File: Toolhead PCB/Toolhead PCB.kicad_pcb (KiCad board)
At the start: 2 copper layers, 37.6 x 23.5 mm, 10 parts, among them J1 PicoA, J10 Conn_02x04_Odd_Even, J2 PicoB, J3 PicoC, J4 Heater, J5 Thermistor, J6 Heatbreak Fan, J7 Part Fan, J8 IR/ADXL, J9 MicroProbe

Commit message: Moved the hole for the capacitor down by 0.4mm, and enlarged diameter by 0.5mm. Updated Edge Cuts circle to match. Exported Gerbers and Excellon files. Basic FlatCAM with B_Cu.gbr, Edge_Cuts.gbr, and PTH.drl mirrored along X axis of Edge_Cuts.gbr. Added Alignment Holes. Set Origin.
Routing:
- net Net-(J3-Pin_6): vias 0 -> 1
- net (no net): vias 3 -> 2
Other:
- outline, holes or cut-outs redrawn
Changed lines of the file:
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@@
 	)
 	(gr_circle
-		(center 117.45 52.4)
-		(end 119.5 52.4)
+		(center 117.45 52.8)
+		(end 119.75 52.8)
 		(stroke
 			(width 0.05)
-			(type default)
+			(type solid)
 		)
 		(fill no)
@@
 	(via
 		(at 126.25 65.5)
-		(size 3.126)
+		(size 3.125001)
 		(drill 3.125)
 		(layers "F.Cu" "B.Cu")
@@
 	)
 	(via
-		(at 117.45 52.4)
-		(size 4.001)
-		(drill 4)
-		(layers "F.Cu" "B.Cu")
-		(net 0)
-	)
-	(via
 		(at 107.75 65.5)
-		(size 3.126)
+		(size 3.125001)
 		(drill 3.125)
 		(layers "F.Cu" "B.Cu")
@@
 		(net 5)
 	)
+	(via
+		(at 117.45 52.8)
+		(size 4.500001)
+		(drill 4.5)
+		(layers "F.Cu" "B.Cu")
+		(net 5)
+	)

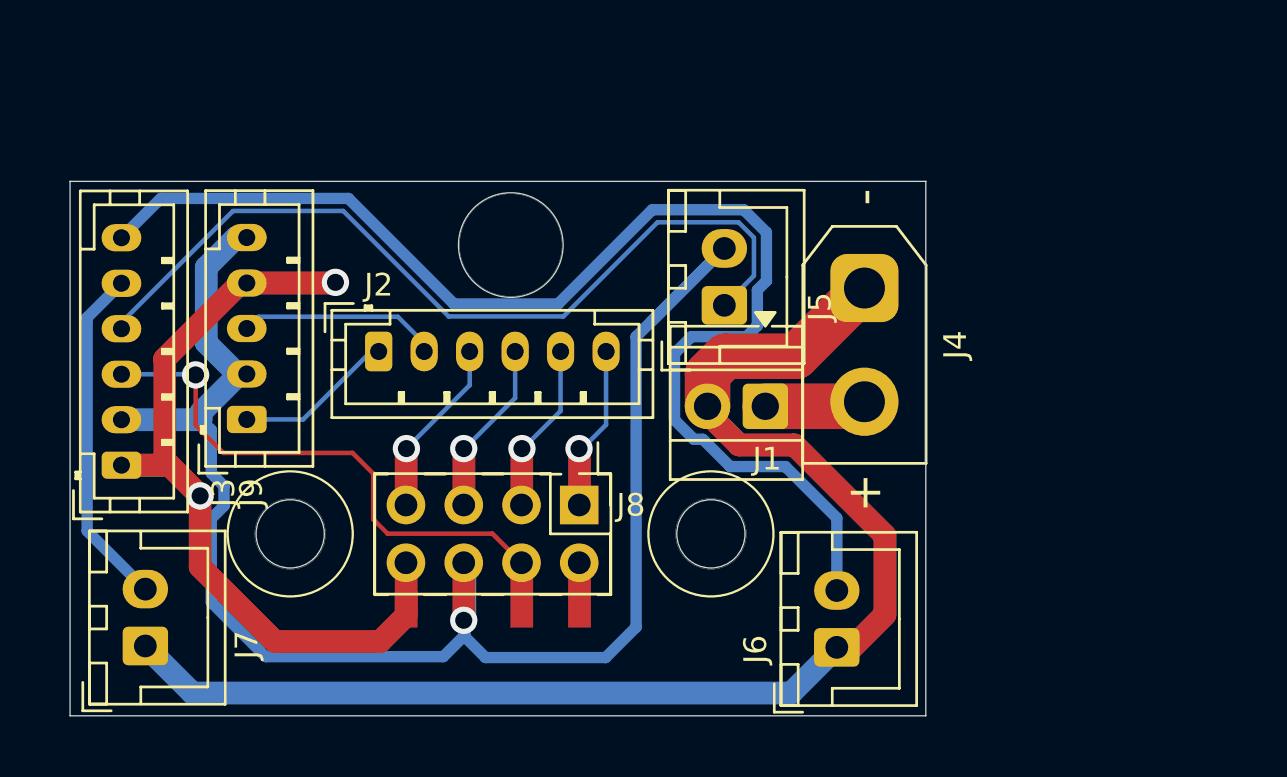
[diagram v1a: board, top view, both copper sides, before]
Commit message: Created symbol and footprint for the Muon 3D IR Bed Probe with ADXL345.
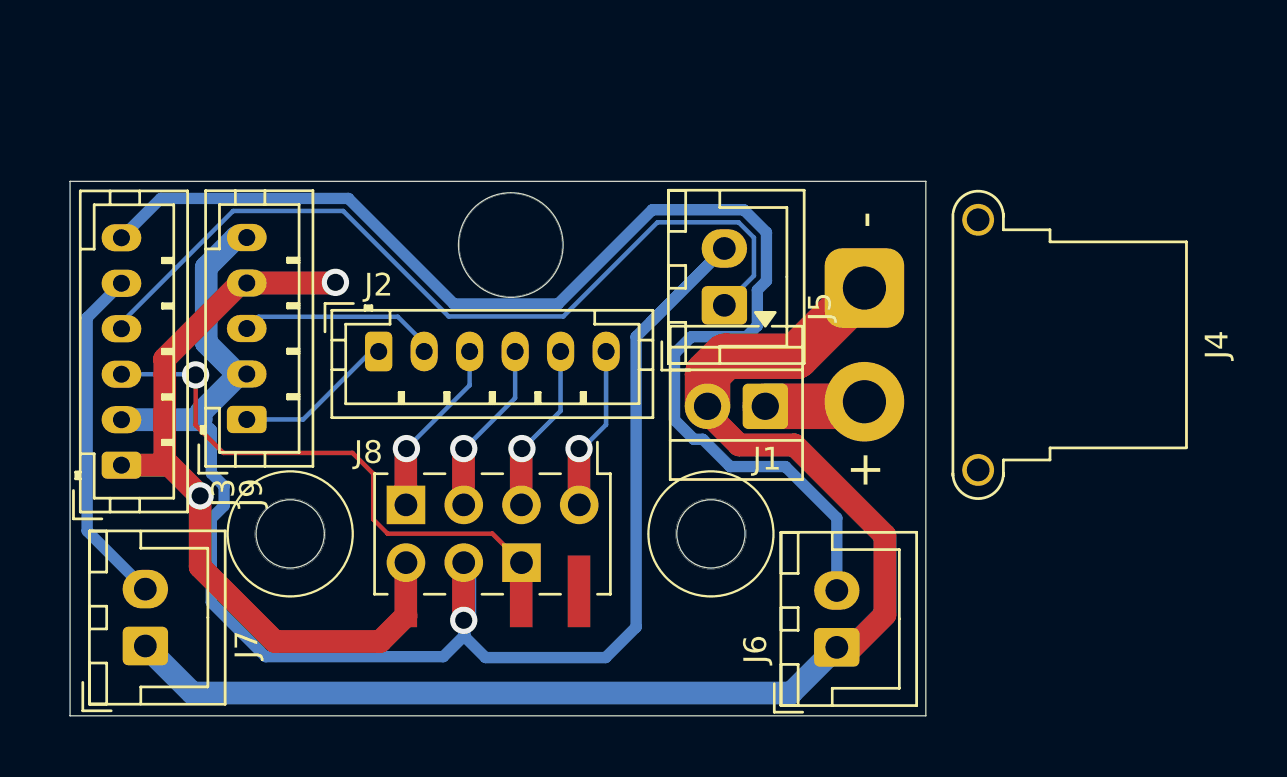
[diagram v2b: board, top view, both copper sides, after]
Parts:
- removed J10: Conn_02x04_Odd_Even, Connector_PinHeader_2.54mm:PinHeader_2x04_P2.54mm_Vertical
- J4: footprint Connector_AMASS:AMASS_XT30UPB-F_1x02_P5.0mm_Vertical -> Connector_AMASS:AMASS_XT30PW-F_1x02_P2.50mm_Horizontal
- J8: footprint Connector_PinHeader_2.54mm:PinHeader_2x04_P2.54mm_Vertical_SMD -> Positron V3:Muon 3D IR Bed Probe with ADXL345
- moved J8 4.16 mm to (115.0, 61.7), turned to 0 degrees
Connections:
- J2 pad 3: Net-(J10-Pin_7) -> Net-(J2-Pin_3)
- J2 pad 5: Net-(J10-Pin_3) -> Net-(J2-Pin_5)
- J2 pad 6: Net-(J10-Pin_1) -> Net-(J2-Pin_6)
- J3 pad 1: Net-(J10-Pin_8) -> Net-(J3-Pin_1)
- J3 pad 2: Net-(J10-Pin_6) -> Net-(J3-Pin_2)
- J3 pad 3: Net-(J10-Pin_4) -> Net-(J3-Pin_3)
- J5 pad 2: Net-(J10-Pin_6) -> Net-(J3-Pin_2)
- J8 pad 1: Net-(J10-Pin_1) -> Net-(J3-Pin_3)
- J8 pad 2: Net-(J10-Pin_2) -> Net-(J3-Pin_2)
- J8 pad 3: Net-(J10-Pin_3) -> Net-(J3-Pin_1)
- J8 pad 4: Net-(J10-Pin_4) -> Net-(J2-Pin_3)
- J8 pad 6: Net-(J10-Pin_6) -> Net-(J2-Pin_5)
- J8 pad 7: Net-(J10-Pin_7) -> Net-(J2-Pin_6)
- J9 pad 2: Net-(J10-Pin_6) -> Net-(J3-Pin_2)
- J9 pad 4: Net-(J10-Pin_8) -> Net-(J3-Pin_1)
- J9 pad 5: Net-(J10-Pin_6) -> Net-(J3-Pin_2)
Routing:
- net Net-(J3-Pin_2): track 0.00 -> 74.2 mm, vias 0 -> 1
- net Net-(J10-Pin_6): track 74.2 -> 0.00 mm, vias 1 -> 0
- net Net-(J10-Pin_8): track 40.7 -> 0.00 mm, vias 2 -> 0
- net Net-(J3-Pin_1): track 0.00 -> 39.6 mm, vias 0 -> 2
- net Net-(J3-Pin_3): track 0.00 -> 23.5 mm, vias 0 -> 1
- net Net-(J10-Pin_4): track 23.5 -> 0.00 mm, vias 1 -> 0
- net Net-(J10-Pin_7): track 7.54 -> 0.00 mm, vias 1 -> 0
- net Net-(J10-Pin_3): track 7.52 -> 0.00 mm, vias 1 -> 0
- net Net-(J10-Pin_1): track 6.29 -> 0.00 mm, vias 1 -> 0
- net Net-(J2-Pin_3): track 0.00 -> 5.41 mm, vias 0 -> 1
- net Net-(J2-Pin_5): track 0.00 -> 5.02 mm, vias 0 -> 1
- net Net-(J2-Pin_6): track 0.00 -> 4.87 mm, vias 0 -> 1
- net Net-(J2-Pin_4): track 8.94 -> 5.28 mm

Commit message: Labeled all the pins/nets. Moved connector Values to F.Silkscreen and moved connector References to F.Fab.
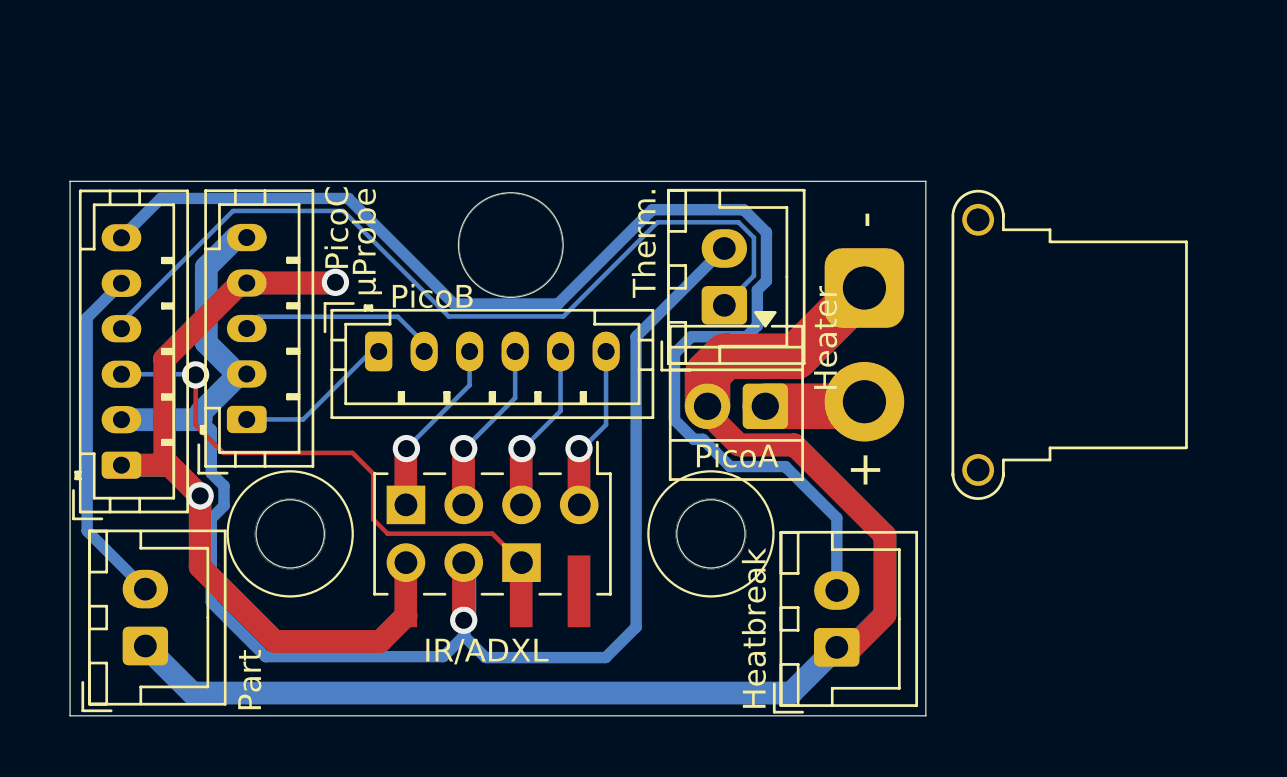
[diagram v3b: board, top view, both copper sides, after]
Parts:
- J5: value Thermistor -> Therm.
- J6: value Heatbreak Fan -> Heatbreak
- J7: value Part Fan -> Part
- J9: value MicroProbe -> µProbe
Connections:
- net Net-(J1-Pin_1) renamed /Heater-
- net Net-(J1-Pin_2) renamed /+24V
- net Net-(J2-Pin_1) renamed /µProbe
- net Net-(J2-Pin_2) renamed /Servo
- net Net-(J2-Pin_3) renamed /CS
- net Net-(J2-Pin_4) renamed /MI
- net Net-(J2-Pin_5) renamed /MO
- net Net-(J2-Pin_6) renamed /SC
- net Net-(J3-Pin_1) renamed /5V
- net Net-(J3-Pin_2) renamed /GND
- net Net-(J3-Pin_3) renamed /Z-Stop
- net Net-(J3-Pin_4) renamed /TH0+
- net Net-(J3-Pin_5) renamed /FAN3- Part
- net Net-(J3-Pin_6) renamed /FAN2- Heatbreak
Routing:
- net /GND: track 74.2 -> 66.8 mm

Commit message: Redesigned PCB: - narrower so it does not protrude as much past the boundary when the Positron is packed for storage - all traces on front side only (no more manually soldered vias); still recommend fabricating as double-sided so the XT30 connector can be soldered on both sides - uses soldered wires to save space
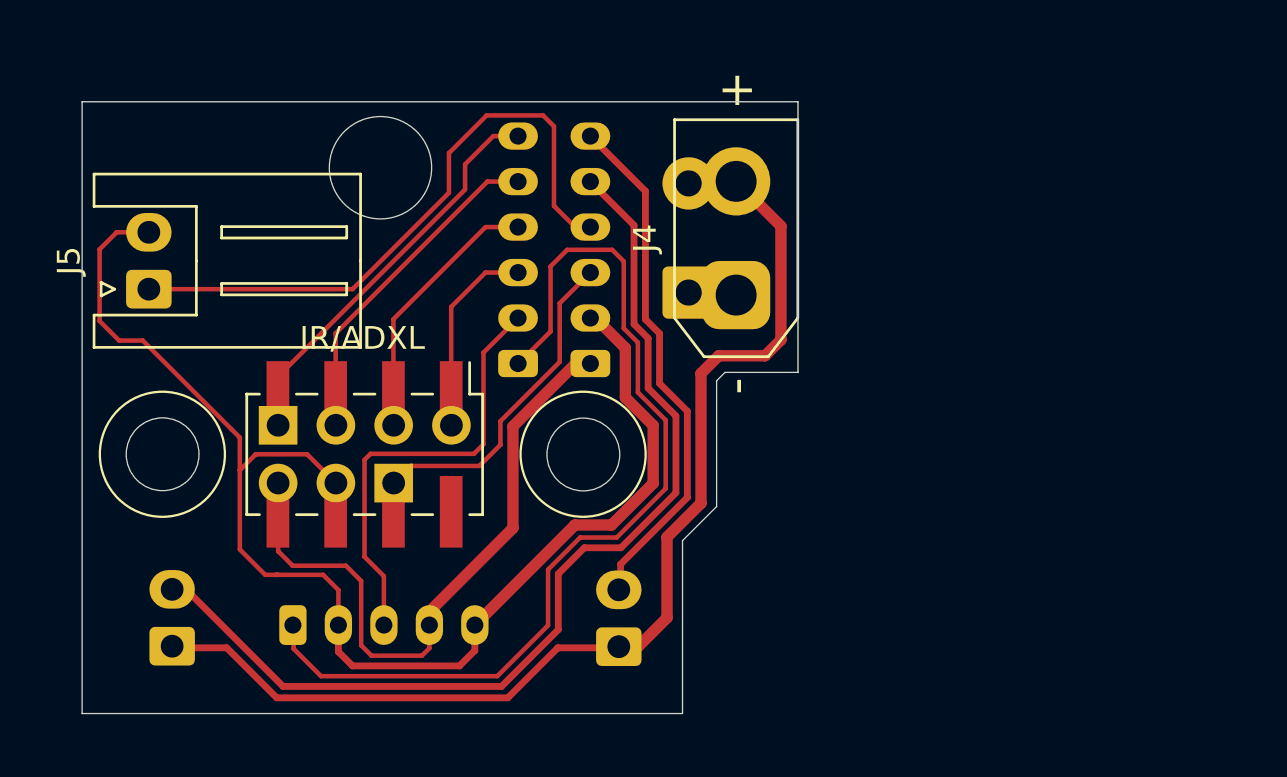
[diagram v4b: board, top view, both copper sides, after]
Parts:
- added Hole: Hole 3.2mm, MountingHole:MountingHole_3.2mm_M3, F.Cu at (120.6, 62.0)
- added Hole: Capacitor Hole 4.5mm, MountingHole:MountingHole_4.5mm, F.Cu at (111.7, 49.4)
- added Hole: Hole 3.2mm, MountingHole:MountingHole_3.2mm_M3, F.Cu at (102.1, 62.0)
- J1: footprint TerminalBlock:TerminalBlock_Xinya_XY308-2.54-2P_1x02_P2.54mm_Horizontal -> Connector_Wire:SolderWire-0.5sqmm_1x02_P4.8mm_D0.9mm_OD2.3mm; moved to B.Cu
- J2, J3, J6, J7, J9: moved to B.Cu
- J4: footprint Connector_AMASS:AMASS_XT30PW-F_1x02_P2.50mm_Horizontal -> Connector_AMASS:AMASS_XT30UPB-M_1x02_P5.0mm_Vertical
- J5: footprint Connector_JST:JST_XH_B2B-XH-A_1x02_P2.50mm_Vertical -> Connector_JST:JST_XH_S2B-XH-A_1x02_P2.50mm_Horizontal
- moved J5 25.3 mm to (101.5, 54.7)
- moved J3 21.1 mm to (120.9, 58.0)
- moved J6 9.59 mm to (122.2, 70.5)
- moved J9 9.26 mm to (107.9, 69.5), turned to 0 degrees
- moved J8 6.62 mm to (109.3, 58.2)
- moved J2 6.15 mm to (117.8, 58.0), turned to 90 degrees
- moved J1 6.03 mm to (125.3, 54.9), turned to 90 degrees
- moved J4 5.65 mm to (127.4, 55.0), turned to 90 degrees
- moved J7 1.18 mm to (102.6, 70.4)
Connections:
- J2 pad 3: /CS -> /SC
- J2 pad 4: /MI -> /MO
- J2 pad 5: /MO -> /MI
- J2 pad 6: /SC -> /CS
- J4 pad 1: /+24V -> /Heater-
- J4 pad 2: /Heater- -> /+24V
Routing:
- net /+24V: track 85.7 -> 49.8 mm
- net /µProbe: track 7.04 -> 42.1 mm
- net /FAN2- Heatbreak: track 56.6 -> 23.0 mm, vias 1 -> 0
- net /FAN3- Part: track 15.1 -> 44.1 mm
- net /CS: track 5.41 -> 16.5 mm, vias 1 -> 0
- net /Servo: track 8.86 -> 19.3 mm
- net /TH0+: track 37.9 -> 27.7 mm
- net /Heater-: track 9.20 -> 0.00 mm
- net /Z-Stop: track 23.5 -> 14.6 mm, vias 1 -> 0
- net /MI: track 5.28 -> 13.7 mm, vias 1 -> 0
- net /GND: track 66.8 -> 58.8 mm, vias 1 -> 0
- net /5V: track 39.6 -> 32.0 mm, vias 2 -> 0
- net /MO: track 5.02 -> 10.6 mm, vias 1 -> 0
- net /SC: track 4.87 -> 7.55 mm, vias 1 -> 0
- net (no net): vias 2 -> 0
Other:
- board size 37.6 x 23.5 mm -> 31.5 x 26.9 mm

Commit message: Changed Silkscreen labels.
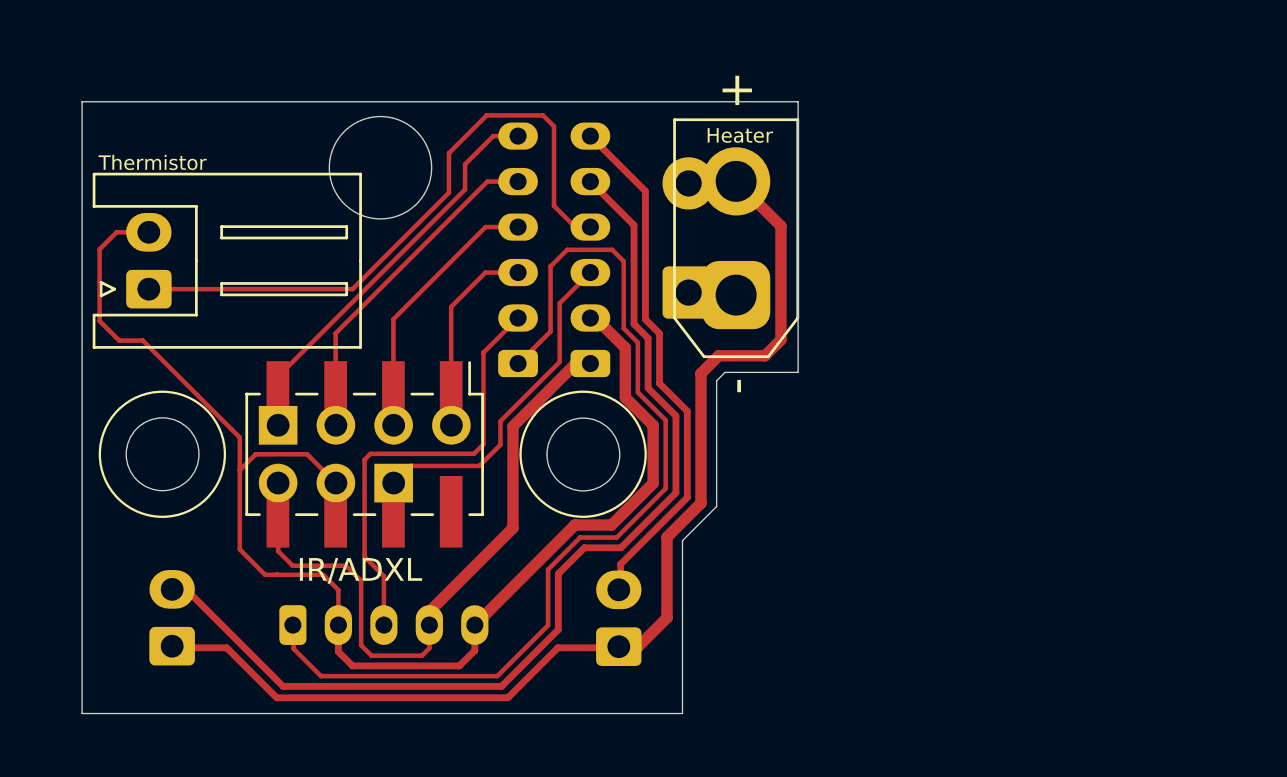
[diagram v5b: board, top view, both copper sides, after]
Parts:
- J5: value Therm. -> Thermistor
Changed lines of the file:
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@@
 			(at 2.5 -4 90)
 			(layer "F.SilkS")
+			(hide yes)
 			(effects
 				(font
@@
 		)
 		(property "Value" "Heater"
-			(at 2.5 4 90)
-			(layer "F.Fab")
-			(effects
-				(font
-					(size 1 1)
+			(at 7 0.140584 180)
+			(layer "F.SilkS")
+			(effects
+				(font
+					(size 0.635 0.635)
 					(thickness 0.15)
 				)
@@
 			(at 1.25 -3.51 90)
 			(layer "F.SilkS")
+			(hide yes)
 			(effects
 				(font
@@
 			)
 		)
-		(property "Value" "Therm."
-			(at 1.25 10.4 90)
-			(layer "F.Fab")
-			(effects
-				(font
-					(size 1 1)
+		(property "Value" "Thermistor"
+			(at 5.54 0.165584 180)
+			(layer "F.SilkS")
+			(effects
+				(font
+					(size 0.635 0.635)
 					(thickness 0.15)
 				)
@@
 		)
 		(property "Value" "IR/ADXL"
-			(at 1.58 -1.325 0)
+			(at 1.460584 8.875 0)
 			(layer "F.SilkS")
 			(effects
@@
 		(model "${KICAD9_3DMODEL_DIR}/Connector_PinHeader_2.54mm.3dshapes/PinHeader_2x04_P2.54mm_Vertical.step"
 			(offset
-				(xyz 0 0 0)
+				(xyz -2 -5 -4)
 			)
 			(scale
@@
 			)
 			(rotate
-				(xyz 0 0 0)
+				(xyz -0 -0 -90)
 			)
 		)
@@
 			(at 0.61 2.550584 90)
 			(layer "B.SilkS")
+			(hide yes)
 			(effects
 				(font
@@
 		)
 		(property "Value" "PicoC"
-			(at 5.61 1.450584 90)
-			(layer "B.Fab")
-			(effects
-				(font
-					(size 1 1)
+			(at 8.11 1.350584 90)
+			(layer "B.SilkS")
+			(effects
+				(font
+					(size 0.635 0.635)
 					(thickness 0.15)
 				)
@@
 		(sheetname "/")
 		(sheetfile "Toolhead PCB.kicad_sch")
-		(attr through_hole)
+		(attr through_hole allow_missing_courtyard)
 		(fp_line
 			(start 12.06 -2.91)
@@
 			(at -2.11 0.030584 90)
 			(layer "B.SilkS")
+			(hide yes)
 			(effects
 				(font
@@
 		)
 		(property "Value" "PicoA"
-			(at 2.59 -1.069416 90)
-			(layer "B.Fab")
-			(effects
-				(font
-					(size 1 1)
+			(at 4.99 -1.969416 90)
+			(layer "B.SilkS")
+			(effects
+				(font
+					(size 0.635 0.635)
 					(thickness 0.15)
 				)
@@
 			(at 2.31 -3.569416 90)
 			(layer "B.SilkS")
+			(hide yes)
 			(effects
 				(font
@@
 		)
 		(property "Value" "PicoB"
-			(at 5.51 -1.469416 90)
-			(layer "B.Fab")
-			(effects
-				(font
-					(size 1 1)
+			(at 8.11 1.130584 90)
+			(layer "B.SilkS")
+			(effects
+				(font
+					(size 0.635 0.635)
 					(thickness 0.15)
 				)
@@
 		(sheetname "/")
 		(sheetfile "Toolhead PCB.kicad_sch")
-		(attr through_hole)
+		(attr through_hole allow_missing_courtyard)
 		(fp_line
 			(start 12.06 -2.91)

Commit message: Widened traces to tolerate overmilling.
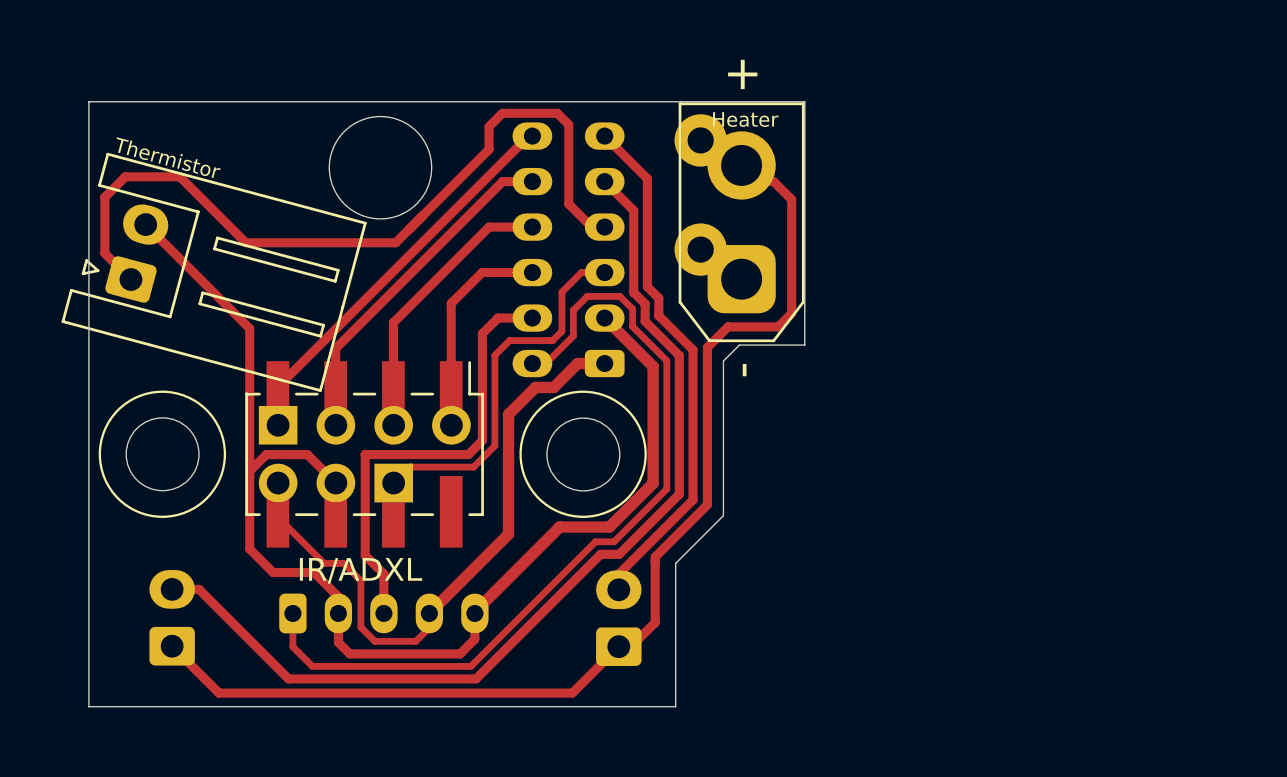
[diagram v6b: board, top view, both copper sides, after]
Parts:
- moved J1 1.96 mm to (125.8, 53.0)
- moved J5 0.89 mm to (100.7, 54.3), turned to 75 degrees
- moved J4 0.74 mm to (127.6, 54.3)
- moved J2 0.63 mm to (118.4, 58.0)
- moved J3 0.63 mm to (121.6, 58.0)
- moved J9 0.51 mm to (107.9, 69.0)
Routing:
- net /TH0+: track 27.7 -> 35.6 mm
- net /µProbe: track 42.1 -> 37.1 mm
- net /GND: track 58.8 -> 55.0 mm
- net /Z-Stop: track 14.6 -> 16.5 mm
- net /FAN3- Part: track 44.1 -> 42.4 mm
- net /SC: track 7.55 -> 8.27 mm
- net /+24V: track 49.8 -> 49.1 mm
- net /CS: track 16.5 -> 17.1 mm
- net /Servo: track 19.3 -> 19.9 mm
- net /MO: track 10.6 -> 11.1 mm
- net /5V: track 32.0 -> 31.5 mm
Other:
- board size 31.5 x 26.9 mm -> 31.5 x 26.6 mm
